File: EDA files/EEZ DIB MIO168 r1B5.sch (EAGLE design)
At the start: 297 parts, among them IC1 M24C32-WMN6P, IC10 DAC7760IPWPR, IC11 DAC7760IPWPR, IC12 OPA376AIDBVR, IC13 DAC7563TDGSR, IC14 OPA2196IDR, IC15 BTS3408G, IC16 BTS3408G, IC17 BTS3408G, IC18 BTS3408G, IC19 74HC126PW,118, IC2 Si8641BB-B-IS1, IC20 TL431B, IC21 DG468DV-T1-E3, IC22 DG468DV-T1-E3, IC23 DG468DV-T1-E3, IC24 DG468DV-T1-E3, IC25 DG468DV-T1-E3, IC26 DG468DV-T1-E3, IC27 DG468DV-T1-E3, IC28 DG468DV-T1-E3, IC29 DG468DV-T1-E3, IC3 Si8641BB-B-IS1, IC30 DG468DV-T1-E3, IC31 DG468DV-T1-E3, IC32 DG468DV-T1-E3, IC33 DG468DV-T1-E3, IC34 DG468DV-T1-E3, IC35 OPA376AIDBVR, IC36 ADS8674IDBT, IC4 L78L12, IC5 LP2985-50DBVR, IC6 LP2985-33DBVR, IC7 L79L12, IC8 STM32F446ZCT6, IC9 OPA2196IDR, J1 4907, J2 N.C., Q1 2N7002PS,115, Q10 BSS169, Q11 BSS169, Q12 BSS169, Q13 BSS169, Q2 2N7002PS,115, Q3 2N7002PS,115, Q4 2N7002PS,115, Q5 2N7002PS,115, Q6 BSS169, Q7 BSS169, Q8 BSS169, Q9 BSS169, X1 77317-104-28LF, X2 SSW-106-02-S-S, X3 691327310016, X4 691327310016, Y1 25MHz

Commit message: Connectors for piggyback, GND and PWM outputs jumpers
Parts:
- removed DIB1.1: JP3-CUT-0805-ROTATED, EEZ_Lib1:JP3-CUT-0805-ROTATED
- removed FB8: BLM18AG102SH1D, EEZ_Lib1:FERRITE_BEAD0603
- removed SH5, SH6, SH7, SH8: (no value), EEZ_Lib1:SHORTNOHOLE
- added JP10, JP12, JP7, JP8: (no value), EEZ_Lib1:JUMPER-2PIN-2MM
- added JP11, JP9: JP2-CUT-0805, EEZ_Lib1:JP2-CUT-0805
- added JP6: JP3-CUT-0805-ROTATED, EEZ_Lib1:JP3-CUT-0805-ROTATED
- added L11: BLM18AG102SH1D, EEZ_Lib1:FERRITE_BEAD0603
- added X5, X6, X7: 1-2314878-0, EEZ_connectors:1-2314878-0
- C18: value 4u7 -> 1u
- C19: value 10n -> N.C.
- C20: value 1u -> 18p; device rcl:C-EUC0805 -> rcl:C-EUC0603
- C21: value N.C. -> 18p; device rcl:C-EUC0805 -> rcl:C-EUC0603
- C22: value 18p -> 1n; device rcl:C-EUC0603 -> rcl:C-EUC0805
- C23: value 18p -> 4u7; device rcl:C-EUC0603 -> EEZ_Lib1:ECAP1206
- C24: value 1n -> 100n; device rcl:C-EUC0805 -> rcl:C-EUC0603
- C25: value 4u7 -> 100n; device EEZ_Lib1:ECAP1206 -> rcl:C-EUC0603
- C35, C72, C73, C88: value 100n -> 1u; device rcl:C-EUC0603 -> rcl:C-EUC0805
- C37: value 1u -> 2u2
- C38: value 100n -> 2u2; device rcl:C-EUC0603 -> rcl:C-EUC0805
- C39: value 2u2 -> 2n2
- C40: value 2u2 -> 100n; device rcl:C-EUC0805 -> rcl:C-EUC0603
- C41, C50: value 2n2 -> 100n; device rcl:C-EUC0805 -> rcl:C-EUC0603
- C42, C51: value 100n -> 22n; device rcl:C-EUC0603 -> rcl:C-EUC0805
- C44, C53: value 22n -> 100n; device rcl:C-EUC0805 -> rcl:C-EUC0603
- C46, C47, C57, C58, C64: value 100n -> 4u7; device rcl:C-EUC0603 -> rcl:C-EUC0805
- C48: value 4u7 -> 2n2
- C49, C59, C60, C66: value 4u7 -> 100n; device rcl:C-EUC0805 -> rcl:C-EUC0603
- C61: value 100n -> 150n; device rcl:C-EUC0603 -> rcl:C-EUC0805
- C63: value 150n -> 100n; device rcl:C-EUC0805 -> rcl:C-EUC0603
- C86: value 1u -> 100n; device rcl:C-EUC0805 -> rcl:C-EUC0603
- C89: value 2n2 -> 4n7/1kV; device rcl:C-EUC0805 -> rcl:C-EUC1812
- C90, C97: value 2n2 -> 1n
- C91: value 10u -> 1n; device rcl:C-EUC1206 -> rcl:C-EUC0805
- C92: value 1u -> 10u; device rcl:C-EUC0805 -> rcl:C-EUC1206
- C93: value 22u -> 1u; device rcl:C-EUC1206 -> rcl:C-EUC0805
- C94: value 10u -> 22u
- C96: value 2n2 -> 10u; device rcl:C-EUC0805 -> rcl:C-EUC1206
- C98: value 4n7/1kV -> 1n; device rcl:C-EUC1812 -> rcl:C-EUC0805
- IC5: value LP2985-50DBVR -> LM1117MP-5.0; device EEZ_DIB:LP2985 -> EEZ_Lib1:LM1117MP-5.0
- JP1: value JP2-CUT-0805 -> JP3-CUT-0805-ROTATED; device EEZ_Lib1:JP2-CUT-0805 -> EEZ_Lib1:JP3-CUT-0805-ROTATED
- JP3: value JP3-CUT -> JP2-CUT-0805; device EEZ_Lib1:JP3-CUT -> EEZ_Lib1:JP2-CUT-0805
- JP4, JP5: value JP2-CUT-0805 -> DS1025-01-1*3P8BV1-B; device EEZ_Lib1:JP2-CUT-0805 -> EEZ_connectors:JUMPER-3PIN2MM
- R60, R61: value 10K -> 560K; device rcl:R-EU_R0805 -> rcl:R-EU_R1206
- R62: value 47R -> 10K
- R63: value 1K -> 10K
- R66: value N.C. -> 47R
- R67: value N.C. -> 100R
- R68: value 100R -> N.C.
- R69: value 1K1 -> N.C.
- R70, R74, R78: value 47R -> 100R
- R71, R75, R79: value 1K -> 154R
- R72, R76: value 100R -> 47R
- R73, R77: value 1K1 -> 100R
- R80: value 560K -> 47R; device rcl:R-EU_R1206 -> rcl:R-EU_R0805
- R81: value 560K -> 100R; device rcl:R-EU_R1206 -> rcl:R-EU_R0805
- R83: value 1K1 -> 154R
- renumbered FB1 to L4, FB2 to L5, FB3 to L6, FB4 to L7, FB5 to L8, FB6 to L9, FB7 to L10, FB9 to L12, GND to TP1
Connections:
- removed net N$70: C17.2, IC5.BYPASS
- removed net N$90: R76.1, R77.1, SH7.GND_B, TVS7.1
- new net N$39: JP5.2, X3-7.1
- new net N$40: JP5.1, R32.1
- new net N$41: JP7.1, R70.1, R71.1, TVS5.1, X4-2.1, X6-2.1
- net !ADC_CS: now also X5-6.1
- net !RESET: now also C22.1, X5-4.1; no longer C24.1
- net +12V_ISO: now also C45.1, C47.2, C53.1, C58.2, C59.1, C67.2, C68.2, C72.1, JP2.2, JP4.3; no longer C16.2, C47.1, C49.2, C57.1, C60.2, C61.1, C71.2, C72.2, IC5.ON/!OFF, JP1.2
- net +15V_ISO: now also C87.1, JP2.1; no longer C86.1, JP1.1
- net +3V3_ISO: now also C19.1, C41.1, C50.1, C71.2, C96.2, X510.1; no longer C21.1, C43.1, C52.1, C73.2, C95.2
- net +3V3_MCU: now also C22.2, C23.+, C24.1, C25.1; no longer C24.2, C25.+, C35.1, C36.1
- net +5V_ISO: now also C16.2, IC5.VOUT, L11.1, X5-2.1; no longer C18.2, FB8.1
- net -12V_ISO: now also C44.1, C46.2, C54.1, C57.2, C62.1, C73.1, JP3.2, JP5.3, R68.1, R69.1; no longer C46.1, C48.2, C58.1, C59.2, C64.1, JP2.2, R66.1, R67.1
- net -15V_ISO: now also C88.1, JP3.1; no longer C87.1, JP2.1
- net -VSENSE1: now also C40.2; no longer C42.2
- net -VSENSE2: now also C49.2; no longer C51.2
- net 1V25_REF: now also JP6.NO; no longer JP3.NO
- net 2V5_REF: now also C61.2; no longer C63.2
- net ADC_AVDD: now also C86.1, C95.2, L11.2, X5-3.1; no longer C88.1, C94.2, FB8.2
- net ADC_IRQ: now also X5-9.1
- net ADC_MISO: now also X5-8.1
- net ADC_MOSI: now also X5-5.1
- net ADC_SCLK: now also X5-7.1
- net ADC_VREF: now also C92.2, X7-2.1; no longer C91.2
- net AGND2: now also JP8.1, R74.1, R75.1, X4-4.1, X6-6.1; no longer R72.1, R73.1, SH6.GND_B
- net AGND4: now also JP12.1, X4-8.1, X610.1; no longer SH8.GND_B
- net AIN0: now also R62.2; no longer R60.2
- net AIN1: now also R63.2; no longer R61.2
- net AIN_0GND: now also C90.1, R71.2, X7-4.1; no longer C89.1, R69.2
- net AIN_0P: now also C90.2, R64.2, R67.2, X7-3.1; no longer C89.2, R63.2, R66.2
- net AIN_1GND: now also C91.1, R75.2, X7-6.1; no longer C90.1, R73.2
- net AIN_1P: now also C91.2, R65.2, R73.2, X7-5.1; no longer C90.2, R64.2, R71.2
- net AIN_2GND: now also C97.1, R79.2, X7-8.1; no longer C96.1, R77.2
- net AIN_2P: now also C97.2, R68.2, R77.2, X7-7.1; no longer C96.2, R67.2, R75.2
- net AIN_3GND: now also C98.1, X710.1; no longer C97.1
- net AIN_3P: now also C98.2, R69.2, R81.2, X7-9.1; no longer C97.2, R65.2, R79.2
- net DAC_OUT#1: now also C40.1; no longer C42.1
- net DAC_OUT#2: now also C49.1; no longer C51.1
- net DIB_CSB: now also JP1.NO; no longer DIB1.1.NO
- net DIB_IRQ: now also JP1.NC; no longer DIB1.1.NC
- net GND: now also C19.2, C20.1, C21.1, C23.-, C24.2, C25.2, C37.1, C38.1, C41.2, C42.1, C44.2, C46.1, C47.1, C50.2, C51.1, C53.2, C57.1, C58.1, C59.2, C60.2, C61.1, C63.2, C64.1, C66.2, C67.1, C68.1, C72.2, C73.2, C89.2, C96.1, IC5.ADJ/GND, JP10.2, JP12.2, JP7.2, JP8.2, R61.2, X5-1.1, X7-1.1; no longer C18.1, C19.1, C21.2, C22.1, C23.1, C25.-, C37.2, C38.2, C39.1, C40.1, C44.1, C46.2, C47.2, C48.1, C49.1, C53.1, C57.2, C58.2, C59.1, C60.1, C61.2, C63.1, C64.2, C66.1, C67.2, C68.2, C72.1, C73.1, C91.1, C98.2, IC5.GND, R81.2, SH5.GND_A, SH6.GND_A, SH7.GND_A, SH8.GND_A, X4-2.1, X4-4.1, X4-6.1, X4-8.1
- net HART#1: now also C42.2; no longer C44.2
- net HART#2: now also C51.2; no longer C53.2
- net N$106: now also C17.2; no longer C19.2
- net N$11: now also JP1.COM; no longer DIB1.1.COM
- net N$113: now also C38.2; no longer C40.2
- net N$115: now also C35.1, C36.1; no longer C37.1, C38.1
- net N$126: now also R62.1; no longer R60.1
- net N$130: now also R63.1; no longer R61.1
- net N$136: now also JP9.1; no longer JP4.1
- net N$137: now also JP11.1; no longer JP5.1
- net N$19: now also C48.2; no longer C50.2
- net N$2: now also R80.1; no longer R78.1
- net N$20: now also JP6.COM; no longer JP3.COM
- net N$21: now also R60.2, R61.1; no longer R80.2, R81.1
- net N$22: now also JP4.1; no longer X3-6.1
- net N$25: now also JP4.2, X3-6.1; no longer R32.1, X3-7.1
- net N$26: now also C48.1; no longer C50.1
- net N$28: now also JP11.2, R81.1; no longer JP5.2, R79.1
- net N$3: now also JP10.1, R78.1, R79.1, TVS7.1, X4-6.1, X6-8.1; no longer R68.1, R69.1, SH5.GND_B, TVS5.1
- net N$31: now also JP6.NC; no longer JP3.NC
- net N$32: now also R72.1; no longer R70.1
- net N$33: now also R72.2; no longer R70.2
- net N$35: now also C94.2; no longer C92.2
- net N$4: now also R80.2; no longer R78.2
- net N$46: now also C52.1; no longer C54.1
- net N$48: now also C18.2; no longer C20.2
- net N$49: now also C18.1; no longer C20.1
- net N$50: now also R74.2; no longer R72.2
- net N$51: now also R73.1; no longer R71.1
- net N$62: now also C39.2; no longer C41.2
- net N$66: now also C43.1; no longer C45.1
- net N$71: now also C63.1, C64.2; no longer C66.2, C67.1
- net N$73: now also C66.1; no longer C68.1
- net N$74: now also C60.1; no longer C62.1
- net N$77: now also R76.1; no longer R74.1
- net N$78: now also R66.1; no longer R62.1
- net N$82: now also C39.1; no longer C41.1
- net N$84: now also R76.2; no longer R74.2
- net N$85: now also R78.2; no longer R76.2
- net N$86: now also R66.2; no longer R62.2
- net N$87: now also JP9.2, R77.1; no longer JP4.2, R75.1
- net N$89: now also R70.2; no longer R68.2
- net N$91: now also X6-1.1
- net N$92: now also R67.1; no longer R63.1
- net N$93: now also X6-5.1
- net N$94: now also X6-7.1
- net N$96: now also X6-9.1
- net N$97: now also C37.2; no longer C39.2
- net PE: now also C89.1, R60.1; no longer C98.1, R80.1
- net RCC_OSC_IN: now also C20.2; no longer C22.2
- net RCC_OSC_OUT: now also C21.2; no longer C23.2
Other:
- note added: "ADC with switchable voltage/current inputs Temp sensors bias"
- note added: "AIN1+"
- note added: "AIN1-/GND"
- note added: "AIN2+"
- note added: "AIN2-/GND"
- note added: "AIN3+"
- note added: "AIN3-/GND"
- note added: "AIN4+"
- note added: "AIN4-/GND"
- note added: "Analog input type selection (voltage/current)"
- note added: "Bias for two temp. sensors"
- note added: "MCU, optional SDcard"
- note removed: "AIN1"
- note removed: "AIN2"
- note removed: "AIN3"
- note removed: "AIN4"
- note removed: "Analog voltage/current inputs Cold junction compensation"
- note removed: "DIB, EEPROM, Isolated power supply, LDOs"
- moved on the sheet: C16, C17, C18, C21, C22, C24, C26, C27, C28, C29, C30, C31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

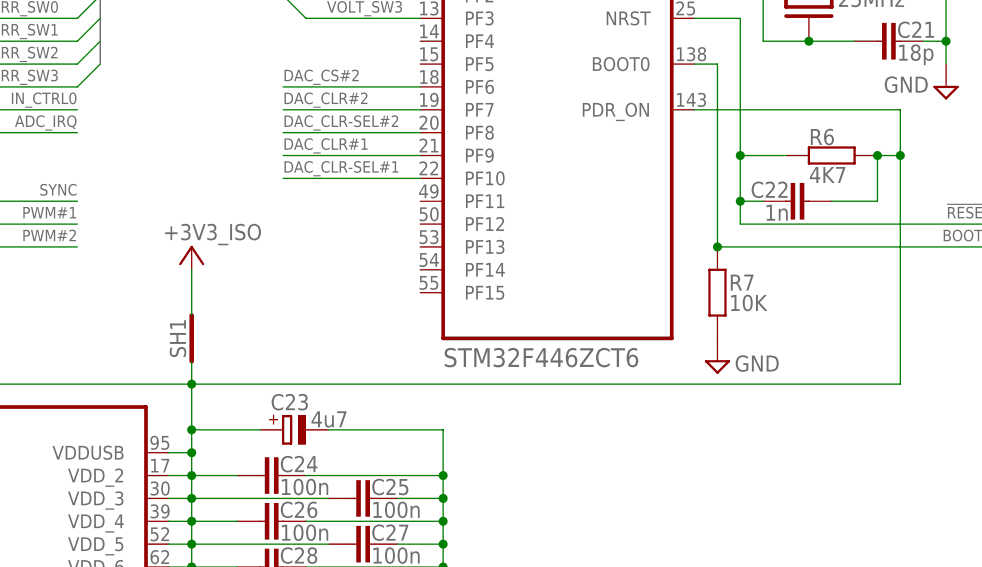
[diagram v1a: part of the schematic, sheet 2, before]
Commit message: MCU Vdd update
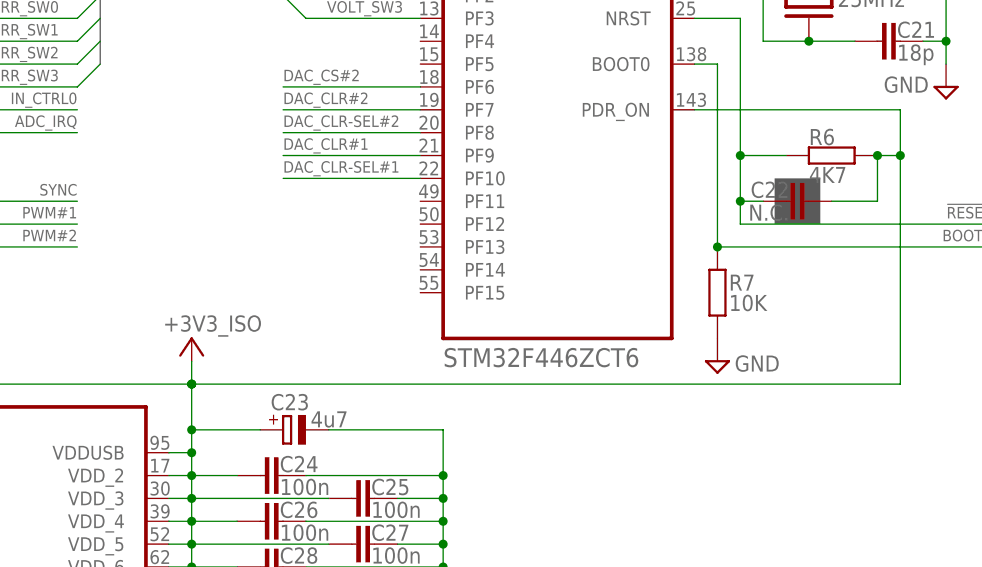
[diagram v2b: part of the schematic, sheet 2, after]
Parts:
- removed SH1: (no value), EEZ_Lib1:SHORTNOHOLE
- C22: value 1n -> N.C.
- JP10, JP12, JP7, JP8: value (none) -> DS1025-01-1*2P8BV1-B
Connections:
- removed net +3V3_MCU: C22.2, C23.+, C24.1, C25.1, C26.1, C27.1, C28.1, C29.1, C30.1, C31.1, C32.1, C33.1, C34.1, IC8B.PDR_ON, IC8C.VBAT, IC8C.VDD, IC8C.VDDUSB, IC8C.VDD_10, IC8C.VDD_11, IC8C.VDD_2, IC8C.VDD_3, IC8C.VDD_4, IC8C.VDD_5, IC8C.VDD_6, IC8C.VDD_7, IC8C.VDD_8, IC8C.VDD_9, L4.1, R6.1, SH1.GND_A
- net +3V3_ISO: now also C22.2, C23.+, C24.1, C25.1, C26.1, C27.1, C28.1, C29.1, C30.1, C31.1, C32.1, C33.1, C34.1, IC8B.PDR_ON, IC8C.VBAT, IC8C.VDD, IC8C.VDDUSB, IC8C.VDD_10, IC8C.VDD_11, IC8C.VDD_2, IC8C.VDD_3, IC8C.VDD_4, IC8C.VDD_5, IC8C.VDD_6, IC8C.VDD_7, IC8C.VDD_8, IC8C.VDD_9, L4.1, R6.1; no longer SH1.GND_B

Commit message: #4, BOM update
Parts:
- removed SH3: (no value), EEZ_Lib1:SHORTNOHOLE
- C40, C49, C60, C66: value 100n -> 1n; device rcl:C-EUC0603 -> rcl:C-EUC0805
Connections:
- removed net -VSENSE1: C40.2, IC10.-VSENSE, SH2.GND_B, TVS1.1
- removed net -VSENSE2: C49.2, IC11.-VSENSE, SH3.GND_B, TVS2.1
- new net -VSENSE: IC10.-VSENSE, IC11.-VSENSE, SH2.GND_B
- net GND: now also C40.2, C49.2, TVS1.1, TVS2.1; no longer SH3.GND_A
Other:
- moved on the sheet: C40, C49, SH2, TVS1, TVS2, X3-1

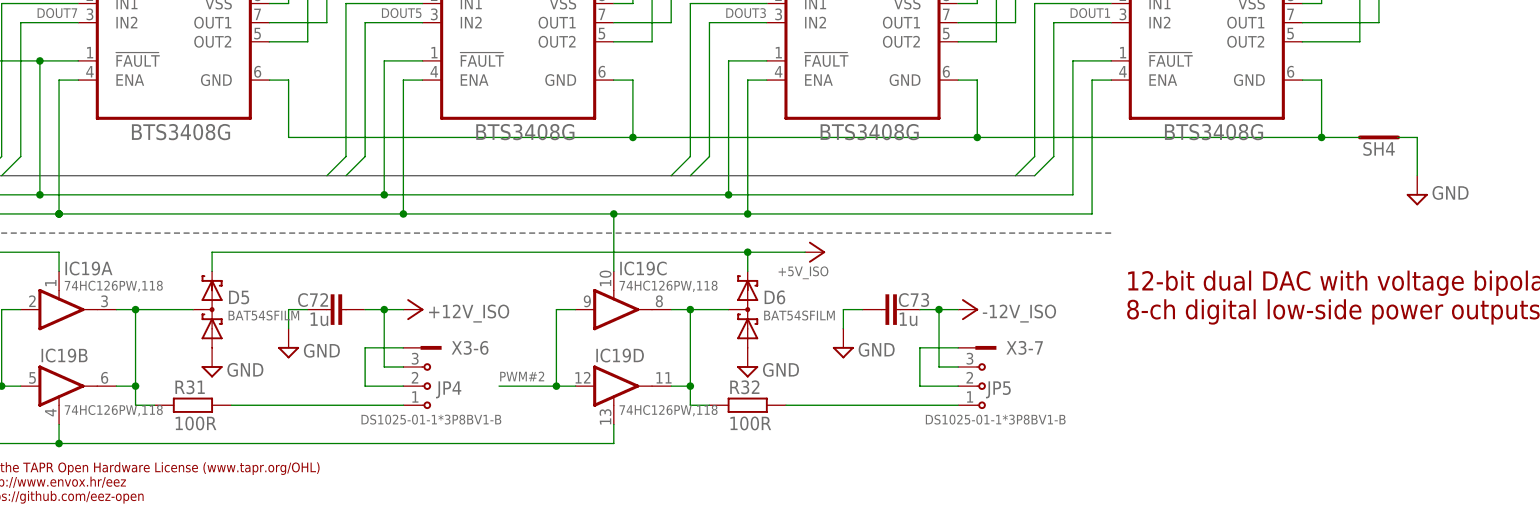
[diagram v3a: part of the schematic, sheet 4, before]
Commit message: ZD1, ZD2 added
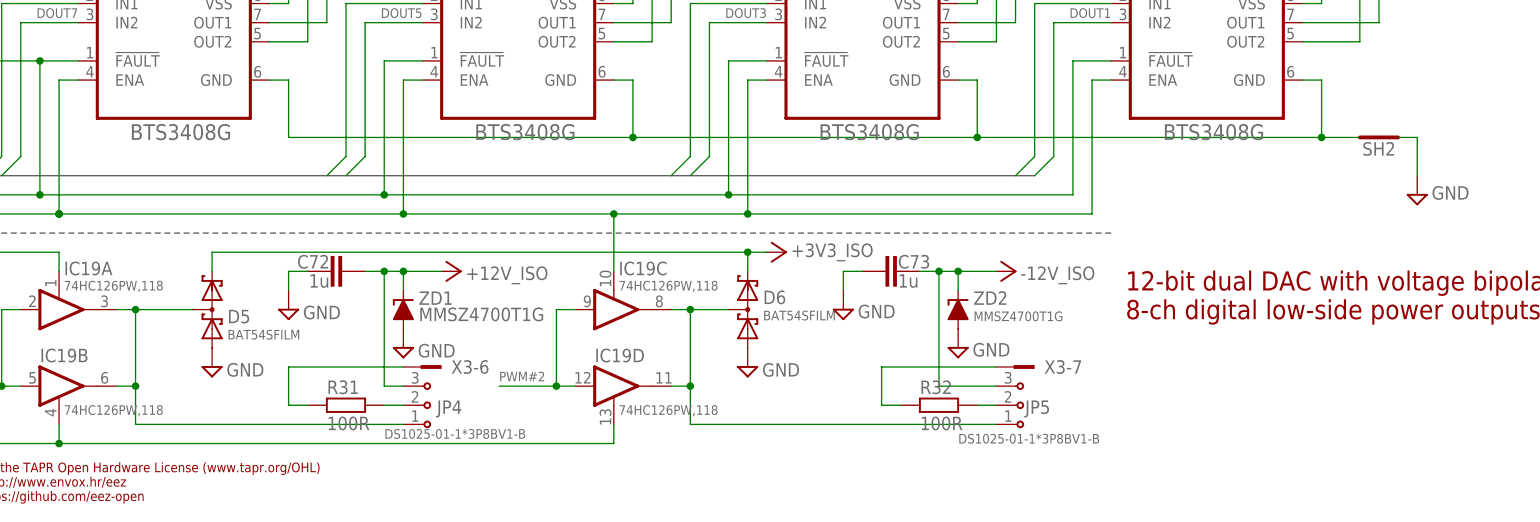
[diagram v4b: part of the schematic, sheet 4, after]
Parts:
- removed SH4: (no value), EEZ_Lib1:SHORTNOHOLE
- added SH1: (no value), EEZ_Lib1:SHORTNOHOLE
- added ZD1, ZD2: MMSZ4700T1G, EEZ_Lib1:ZENER-DIODESOD123
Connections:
- net +12V_ISO: now also ZD1.C
- net +3V3_ISO: now also D5.C2, D6.C2
- net +5V_ISO: no longer D5.C2, D6.C2
- net -12V_ISO: now also ZD2.C
- net -VSENSE: now also SH1.GND_B; no longer SH2.GND_B
- net GND: now also SH1.GND_A, ZD1.A, ZD2.A; no longer SH4.GND_A
- net N$1: now also SH2.GND_B; no longer SH4.GND_B
- net N$129: now also JP4.1; no longer R31.2
- net N$134: now also JP5.1; no longer R32.2
- net N$22: now also JP4.2; no longer JP4.1
- net N$25: now also R31.2; no longer JP4.2
- net N$39: now also R32.2; no longer JP5.2
- net N$40: now also JP5.2; no longer JP5.1
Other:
- moved on the sheet: C72, C73, JP4, JP5, R31, R32, X3-6, X3-7

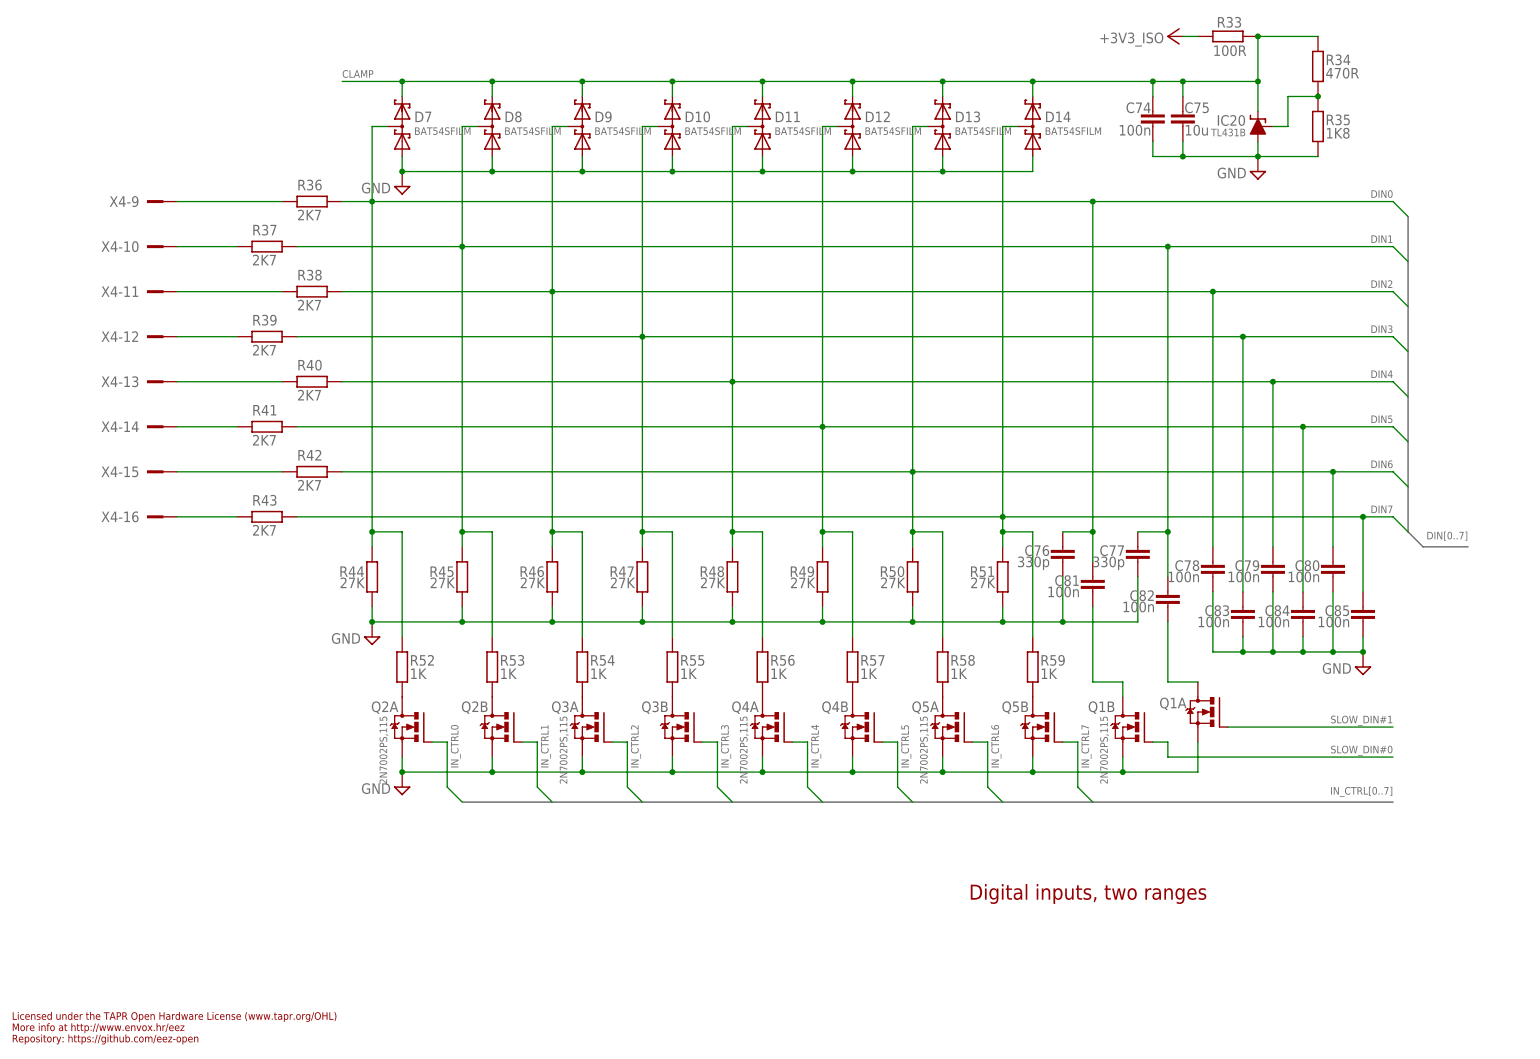
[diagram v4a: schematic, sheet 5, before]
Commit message: PWM outputs pin rearrangement
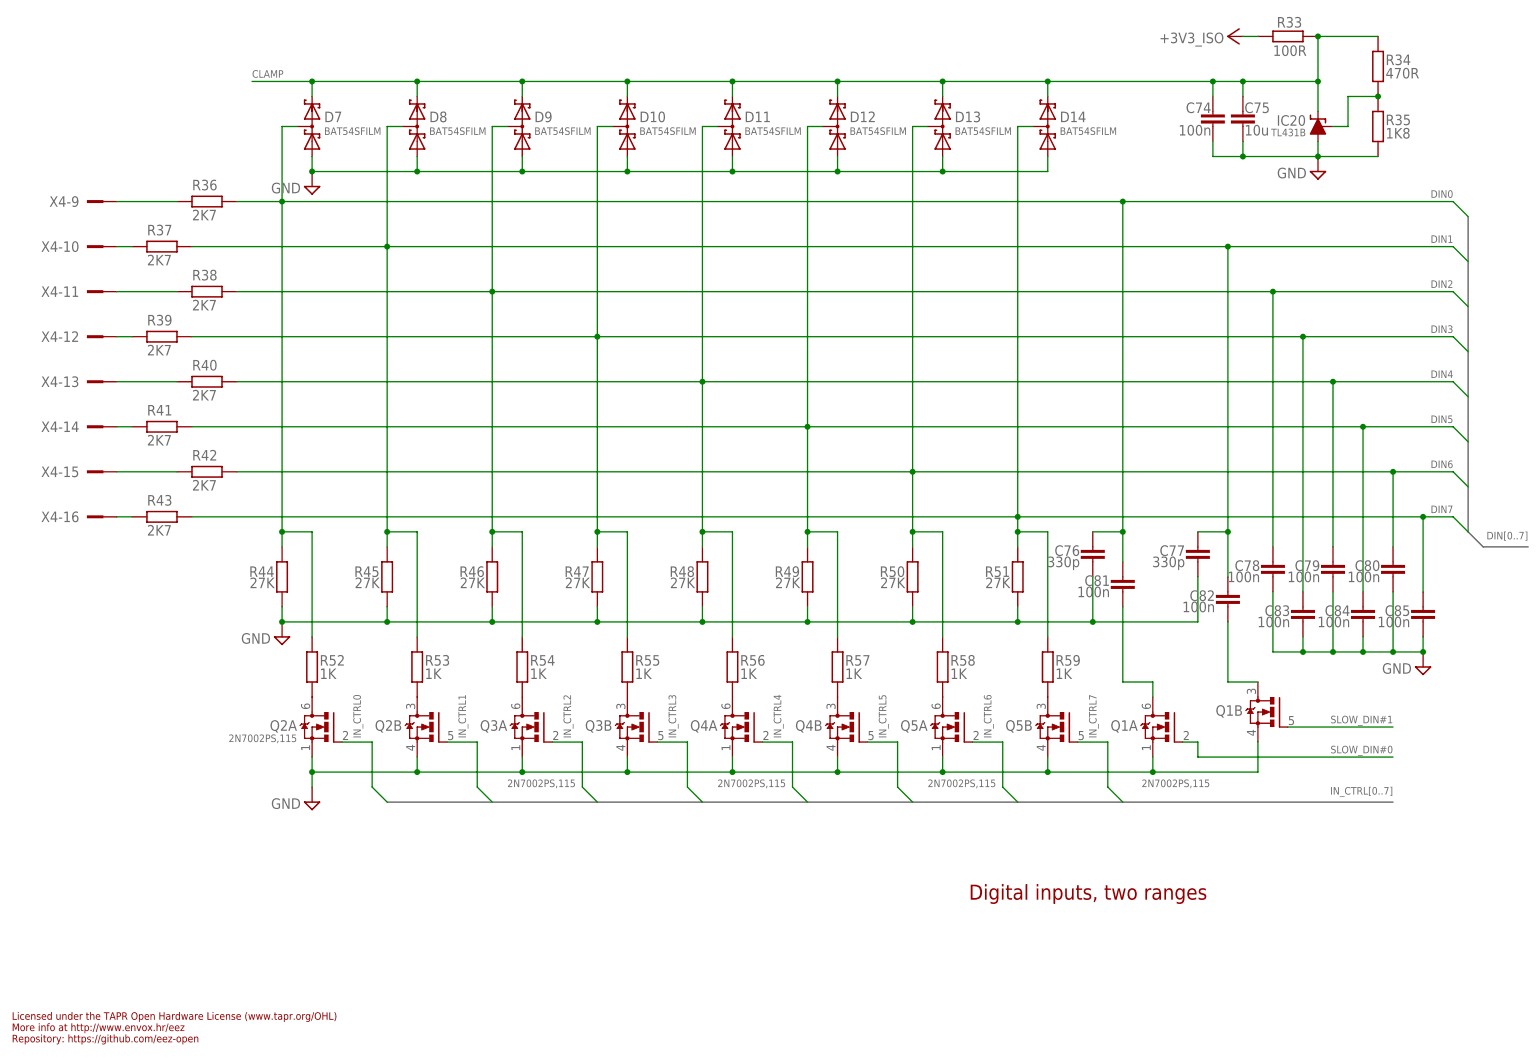
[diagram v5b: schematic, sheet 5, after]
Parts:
- removed C22: N.C., rcl:C-EUC0805
- added FM3: FIDUCIAL_2, EEZ_Lib1:FIDUCIAL_2
- R60, R61: value 560K -> 470K
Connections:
- net N$52 renamed +12V_CM
- net N$53 renamed GND_CM
- net !RESET: no longer C22.1
- net +3V3_ISO: no longer C22.2
- net DOUT1: now also IC8A.PA2; no longer IC8A.PA9
- net N$24: now also Q1A.D; no longer Q1B.D
- net N$76: now also Q1B.D; no longer Q1A.D
- net PWM#2: now also IC8A.PA3; no longer IC8A.PD13
- net SLOW_DIN#0: now also Q1A.G; no longer Q1B.G
- net SLOW_DIN#1: now also Q1B.G; no longer Q1A.G
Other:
- moved on the sheet: C74, C75, C76, C77, C78, C79, C80, C81, C82, C83, C84, C85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
